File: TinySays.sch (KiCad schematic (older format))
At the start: 30 parts, among them IC1 ATTINY85-S, P2 USB_OTG, P3 CONN_01X02, SW1 Switch_SPDT_x2, U1 MCP73831

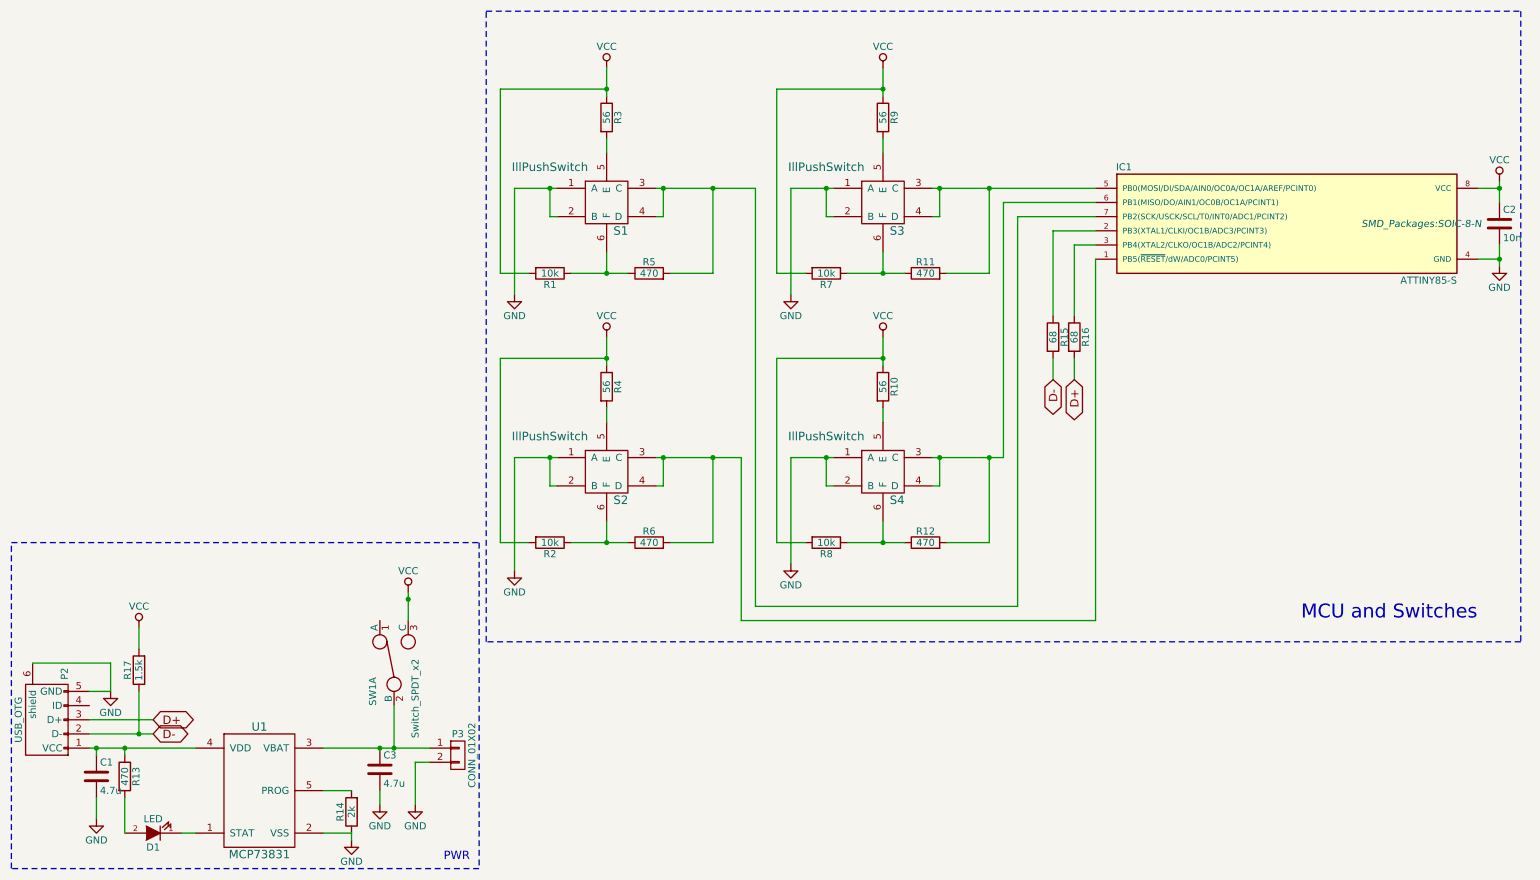
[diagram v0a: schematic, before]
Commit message: PCB v2.0 40mm x 40mm done
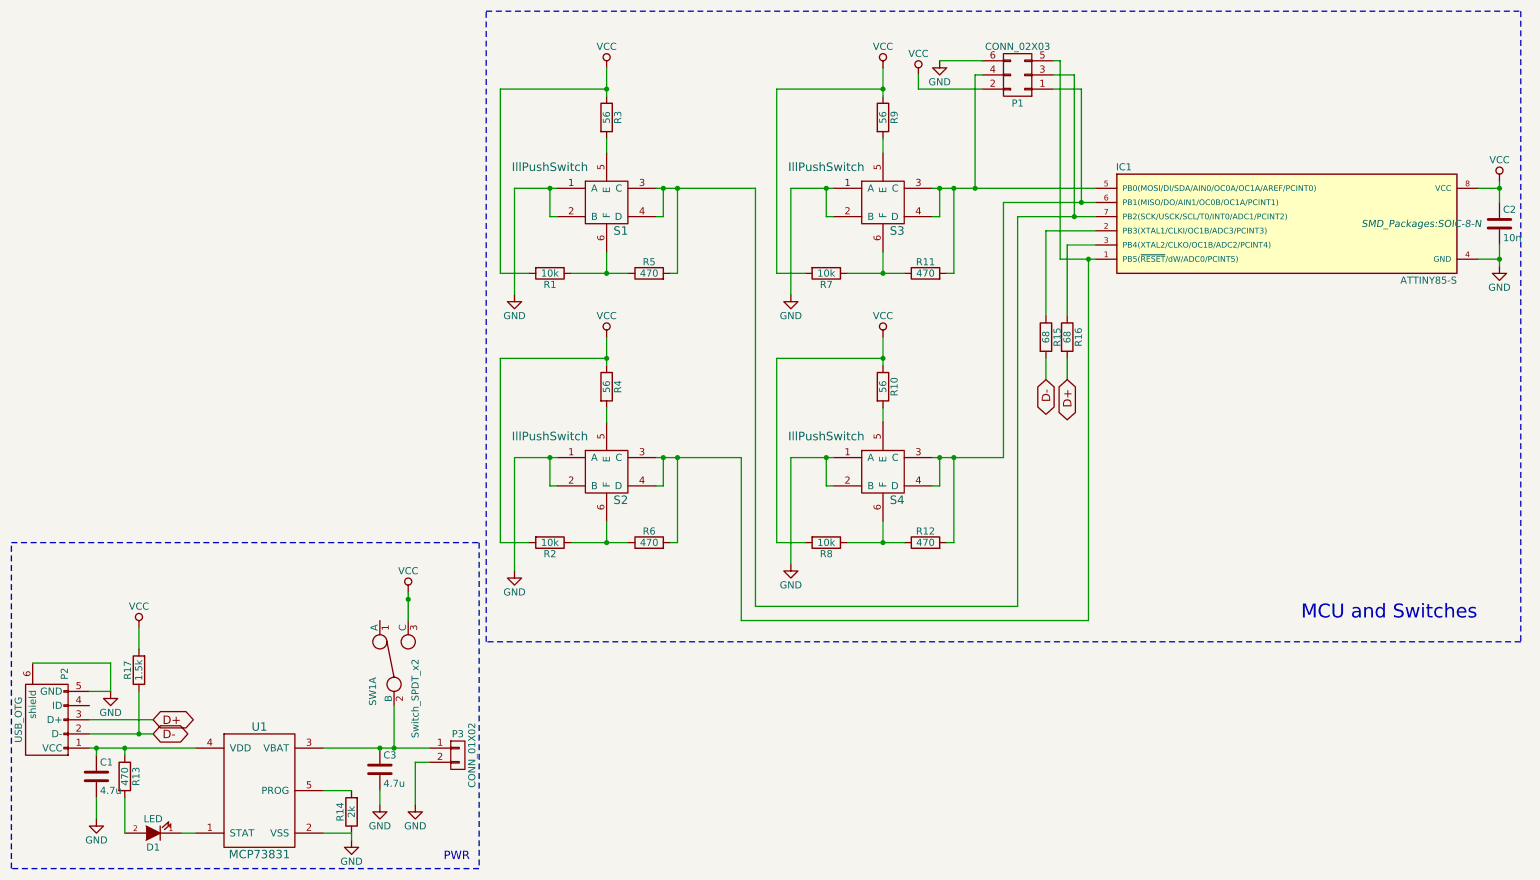
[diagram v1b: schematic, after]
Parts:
- added P1: CONN_02X03, symbol CONN_02X03
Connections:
- net GND: now also P1.6 (P6)
- net VCC: now also P1.2 (P2)
- net at IC1.1 (PB5(~RESET~/dW/ADC0/PCINT5)), R6.2, S2.3 (C)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: now also P1.5 (P5)
- net at IC1.5 (PB0(MOSI/DI/SDA/AIN0/OC0A/OC1A/AREF/PCINT0)), R11.2, S3.3 (C)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: now also P1.4 (P4)
- net at IC1.6 (PB1(MISO/DO/AIN1/OC0B/OC1A/PCINT1)), R12.2, S4.3 (C)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: now also P1.1 (P1)
- net at IC1.7 (PB2(SCK/USCK/SCL/T0/INT0/ADC1/PCINT2)), R5.2, S1.3 (C)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: now also P1.3 (P3)
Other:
- moved on the sheet: R15, R16
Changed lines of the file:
@@
 Text GLabel 1550 6800 2    59   BiDi ~ 0
 D-
-Text GLabel 8050 4300 3    59   BiDi ~ 0
+Text GLabel 8000 4300 3    59   BiDi ~ 0
 D+
-Text GLabel 7900 4300 3    59   BiDi ~ 0
+Text GLabel 7850 4300 3    59   BiDi ~ 0
 D-
 $Comp
 L R R15
 U 1 1 571715A7
-P 7900 4000
-F 0 "R15" V 7980 4000 50  0000 C CNN
-F 1 "68" V 7900 4000 50  0000 C CNN
-F 2 "Resistors_SMD:R_0603_HandSoldering" V 7830 4000 50  0001 C CNN
-F 3 "" H 7900 4000 50  0000 C CNN
-	1    7900 4000
+P 7850 4000
+F 0 "R15" V 7930 4000 50  0000 C CNN
+F 1 "68" V 7850 4000 50  0000 C CNN
+F 2 "Resistors_SMD:R_0603_HandSoldering" V 7780 4000 50  0001 C CNN
+F 3 "" H 7850 4000 50  0000 C CNN
+	1    7850 4000
 	1    0    0    -1
 $EndComp
@@
 L R R16
 U 1 1 57171679
-P 8050 4000
-F 0 "R16" V 8130 4000 50  0000 C CNN
-F 1 "68" V 8050 4000 50  0000 C CNN
-F 2 "Resistors_SMD:R_0603_HandSoldering" V 7980 4000 50  0001 C CNN
-F 3 "" H 8050 4000 50  0000 C CNN
-	1    8050 4000
+P 8000 4000
+F 0 "R16" V 8080 4000 50  0000 C CNN
+F 1 "68" V 8000 4000 50  0000 C CNN
+F 2 "Resistors_SMD:R_0603_HandSoldering" V 7930 4000 50  0001 C CNN
+F 3 "" H 8000 4000 50  0000 C CNN
+	1    8000 4000
 	1    0    0    -1
 $EndComp
@@
 Wire Wire Line
 	7650 5900 7650 3150
-Wire Wire Line
-	8200 6000 8200 3450
 Wire Notes Line
 	550  5450 3850 5450
@@
 	1450 6050 1450 6200
 Wire Wire Line
-	7900 3250 8200 3250
-Wire Wire Line
-	7900 3850 7900 3250
+	7850 3250 8200 3250
+Wire Wire Line
+	7850 3850 7850 3250
 Wire Wire Line
 	7550 3050 8200 3050
 Wire Wire Line
-	8050 3350 8050 3850
-Wire Wire Line
-	7900 4150 7900 4300
-Wire Wire Line
-	8050 4150 8050 4300
+	8000 3350 8000 3850
+Wire Wire Line
+	7850 4150 7850 4300
+Wire Wire Line
+	8000 4150 8000 4300
 Wire Wire Line
 	1100 6800 1550 6800
@@
 Connection ~ 3250 6900
 Wire Wire Line
-	3250 6600 3250 6900
+	3250 6900 3250 6600
 Wire Wire Line
 	3500 7000 3400 7000
@@
 	6350 3150 6300 3150
 Wire Wire Line
-	8050 3350 8200 3350
+	8000 3350 8200 3350
 Wire Notes Line
 	3900 1700 11200 1700
@@
 	11200 1700 11200 6150
 Wire Wire Line
-	5700 6000 8200 6000
+	5700 6000 8150 6000
 Wire Wire Line
 	5800 5900 7650 5900
@@
 	4000 5450 4200 5450
 Wire Wire Line
-	4400 4850 4100 4850
+	4100 4850 4400 4850
 Wire Wire Line
 	4500 5450 4900 5450
@@
 	4750 5450 4750 5300
 Wire Wire Line
-	5500 5450 5200 5450
-Connection ~ 5500 4850
-Wire Wire Line
 	4100 4850 4100 5650
-Wire Wire Line
-	5500 4850 5500 5450
 Wire Wire Line
 	4750 2600 4750 2700
@@
 	4000 3550 4200 3550
 Wire Wire Line
-	4400 2950 4100 2950
+	4100 2950 4400 2950
 Wire Wire Line
 	4500 3550 4900 3550
@@
 	4750 3550 4750 3400
 Wire Wire Line
-	5500 3550 5200 3550
-Connection ~ 5500 2950
-Wire Wire Line
 	4100 2950 4100 3700
-Wire Wire Line
-	5500 2950 5500 3550
 Wire Wire Line
 	6700 4500 6700 4600
@@
 	5950 5450 6150 5450
 Wire Wire Line
-	6350 4850 6050 4850
+	6050 4850 6350 4850
 Wire Wire Line
 	6450 5450 6850 5450
@@
 	6700 5450 6700 5300
 Wire Wire Line
-	7450 5450 7150 5450
-Connection ~ 7450 4850
-Wire Wire Line
 	6050 4850 6050 5600
-Wire Wire Line
-	7450 4850 7450 5450
 Wire Wire Line
 	6700 2600 6700 2700
@@
 	5950 3550 6150 3550
 Wire Wire Line
-	6350 2950 6050 2950
+	6050 2950 6350 2950
 Wire Wire Line
 	7050 2950 8200 2950
@@
 	6700 3550 6700 3400
 Wire Wire Line
-	7450 3550 7150 3550
-Connection ~ 7450 2950
-Wire Wire Line
 	6050 2950 6050 3700
-Wire Wire Line
-	7450 2950 7450 3550
 Text Notes 3600 7700 0    59   ~ 0
 PWR
@@
 	1350 6950 1350 6900
 Connection ~ 1350 6900
+$Comp
+L CONN_02X03 P1
+U 1 1 5718124E
+P 7650 2150
+F 0 "P1" H 7650 2350 50  0000 C CNN
+F 1 "CONN_02X03" H 7650 1950 50  0000 C CNN
+F 2 "" H 7650 950 50  0000 C CNN
+F 3 "" H 7650 950 50  0000 C CNN
+	1    7650 2150
+	-1   0    0    1
+$EndComp
+Wire Wire Line
+	8100 2250 7900 2250
+Wire Wire Line
+	7900 2150 8050 2150
+Wire Wire Line
+	8050 2150 8050 3150
+Connection ~ 8050 3150
+Wire Wire Line
+	8100 2250 8100 3050
+Connection ~ 8100 3050
+Wire Wire Line
+	7900 2050 7950 2050
+Wire Wire Line
+	7950 2050 7950 3450
+Wire Wire Line
+	7950 3450 8200 3450
+Wire Wire Line
+	8150 6000 8150 3450
+Connection ~ 8150 3450
+Wire Wire Line
+	7400 2150 7350 2150
+Wire Wire Line
+	7350 2150 7350 2950
+Connection ~ 7350 2950
+Wire Wire Line
+	7150 3550 7200 3550
+Wire Wire Line
+	7200 3550 7200 2950
+Connection ~ 7200 2950
+Wire Wire Line
+	7150 5450 7200 5450
+Wire Wire Line
+	7200 5450 7200 4850
+Connection ~ 7200 4850
+Wire Wire Line
+	5200 5450 5250 5450
+Wire Wire Line
+	5250 5450 5250 4850
+Connection ~ 5250 4850
+Wire Wire Line
+	5200 3550 5250 3550
+Wire Wire Line
+	5250 3550 5250 2950
+Connection ~ 5250 2950
+$Comp
+L VCC #PWR018
+U 1 1 571889FE
+P 6950 2150
+F 0 "#PWR018" H 6950 2000 50  0001 C CNN
+F 1 "VCC" H 6950 2300 50  0000 C CNN
+F 2 "" H 6950 2150 50  0000 C CNN
+F 3 "" H 6950 2150 50  0000 C CNN
+	1    6950 2150
+	1    0    0    -1
+$EndComp
+$Comp
+L GND #PWR019
+U 1 1 57188A66
+P 7100 2050
+F 0 "#PWR019" H 7100 1800 50  0001 C CNN
+F 1 "GND" H 7100 1900 50  0000 C CNN
+F 2 "" H 7100 2050 50  0000 C CNN
+F 3 "" H 7100 2050 50  0000 C CNN
+	1    7100 2050
+	1    0    0    -1
+$EndComp
+Wire Wire Line
+	7400 2250 6950 2250
+Wire Wire Line
+	6950 2250 6950 2150
+Wire Wire Line
+	7400 2050 7100 2050
 $EndSCHEMATC

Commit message: PCB v2.0 40mm x 40mm done
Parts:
- P1: footprint (none) -> Pin_Headers:Pin_Header_Angled_2x03
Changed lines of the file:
@@
 F 0 "P1" H 7650 2350 50  0000 C CNN
 F 1 "CONN_02X03" H 7650 1950 50  0000 C CNN
-F 2 "" H 7650 950 50  0000 C CNN
+F 2 "Pin_Headers:Pin_Header_Angled_2x03" H 7650 950 50  0001 C CNN
 F 3 "" H 7650 950 50  0000 C CNN
 	1    7650 2150
